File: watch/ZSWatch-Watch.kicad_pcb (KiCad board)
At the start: 4 copper layers, 37.4 x 37.5 mm, 62 parts, among them IC401 nPM1300-QEXX, IC501 APDS-9306-065, IC502 BMI270, IC503 LIS2MDLTR, IC504 BMP581, IC505 DRV2603RUNT, IC506 PCA9306JK, IC507 RV-8263-C8, IC601 FAN5622SX, IC602 USBLC6-2P6, IC603 MX25U51245GZ4I00, IC604 NTS0104GU12, M601 NORA-B106, X402 Battery, X509 Motor, X603 Device, X608 Display

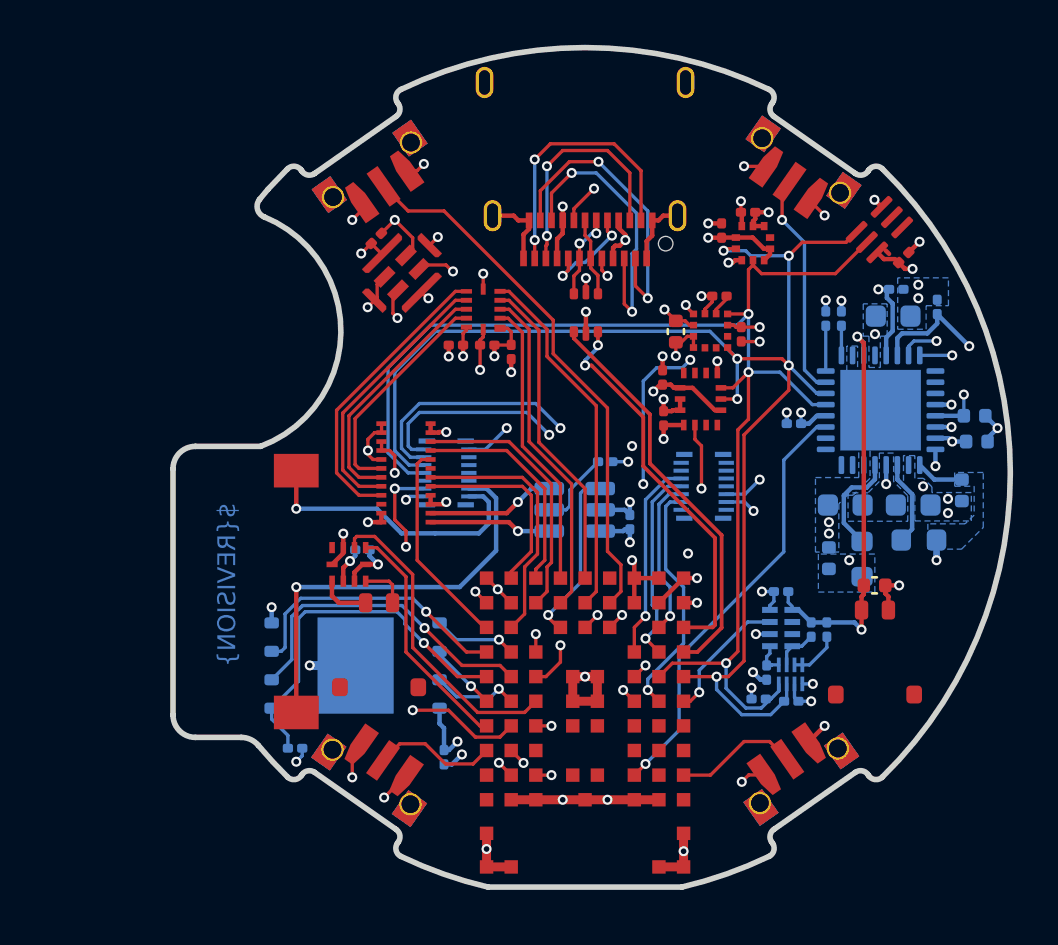
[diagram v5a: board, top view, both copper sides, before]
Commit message: New battery connector
- Add CI/CD workflow to check for changelog updates on pull requests

Signed-off-by: Daniel Kampert <DanielKampert|kampis-elektroecke.de>
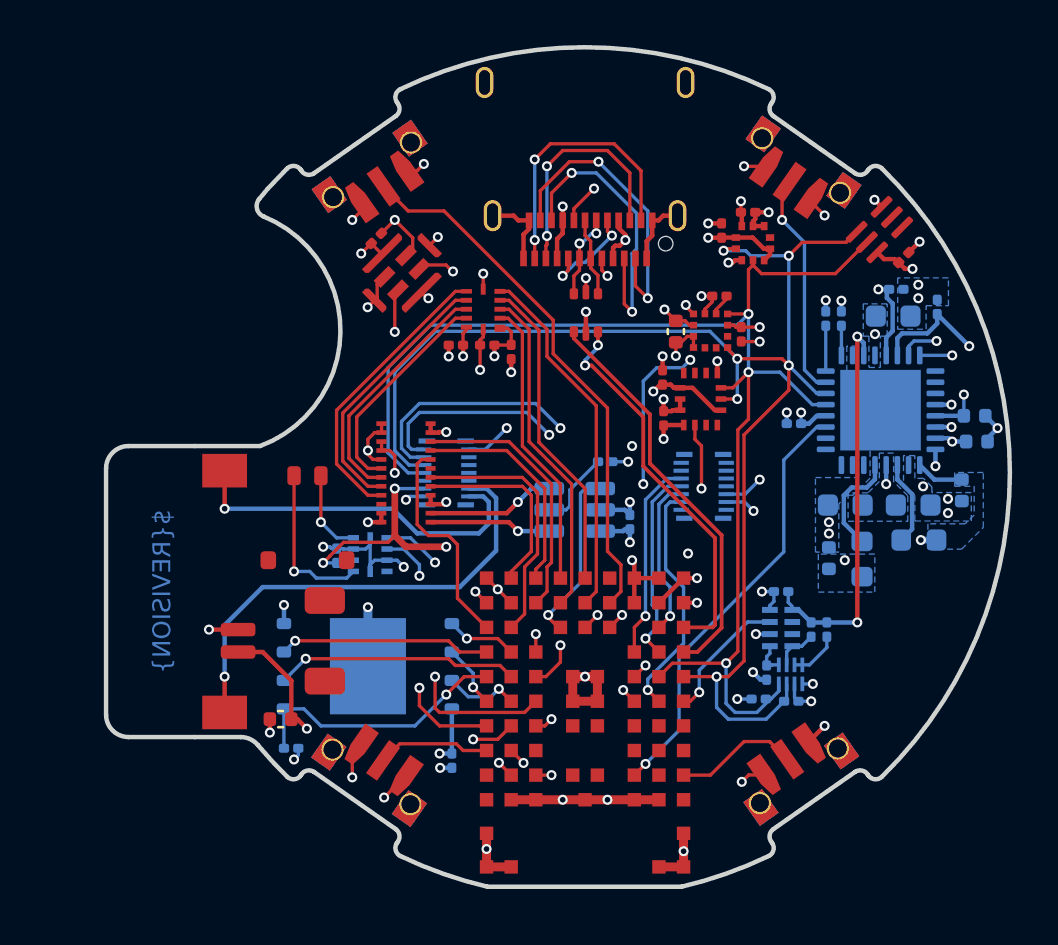
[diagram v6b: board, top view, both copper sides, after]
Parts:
- removed M801: ~, ZSWatch:Extension
- added X701: Conn_02x07_Odd_Even, Amphenol:101P014FB110, B.Cu at (212.3, 139.1)
- added X702: Conn_02x07_Odd_Even, Amphenol:101P014FB110, B.Cu at (200.8, 138.5)
- IC505: moved to B.Cu
- X402: footprint Molex:78171-0002 -> Connector_JST:JST_SH_SM02B-SRSS-TB_1x02-1MP_P1.00mm_Horizontal
- moved C403 27.2 mm to (193.4, 149.5), turned to 180 degrees
- moved X402 26.5 mm to (193.5, 146.0), turned to 90 degrees
- moved X509 6.52 mm to (194.6, 140.5)
- moved LS801 3.20 mm to (188.6, 143.8)
- moved C510 1.18 mm to (195.9, 142.2), turned to 90 degrees
- moved IC505 1.05 mm to (197.4, 142.2), turned to 180 degrees
- moved IC603 0.55 mm to (197.3, 147.1)
- moved C602 0.38 mm to (201.1, 151.4)
- moved R612 0.17 mm to (193.9, 150.8)
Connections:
- M601 pad F3: /Project Architecture/MCU/VIB-PWM -> /Project Architecture/MCU/VIB-EN
- M601 pad G1: /Project Architecture/MCU/VIB-EN -> /Project Architecture/MCU/VIB-PWM
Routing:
- net /Project Architecture/Peripherals/VBAT: track 24.8 -> 54.2 mm, vias 3 -> 4
- net /Project Architecture/MCU/MIC-DATA: track 30.2 -> 37.1 mm
- net Net-(IC505-OUT-): track 2.29 -> 7.17 mm, vias 0 -> 1
- net QSPI-CS: track 16.4 -> 12.0 mm
- net QSPI-IO1: track 14.5 -> 10.9 mm
- net /Project Architecture/MCU/MIC-CLK: track 30.2 -> 33.6 mm
- net /Project Architecture/MCU/VIB-EN: track 10.7 -> 13.9 mm, vias 0 -> 2
- net Net-(X702-Pin_2): track 12.9 -> 16.1 mm
- net QSPI-IO2: track 12.5 -> 9.46 mm
- net /Project Architecture/MCU/VIB-PWM: track 13.9 -> 11.4 mm, vias 0 -> 2
- net Net-(X702-Pin_4): track 18.9 -> 21.1 mm
- net GND: track 77.5 -> 79.2 mm, vias 60 -> 61
- net Net-(IC505-OUT+): track 2.07 -> 3.81 mm, vias 0 -> 1
- net /Project Architecture/Power Management/VSYS: track 57.6 -> 59.2 mm
- net /Project Architecture/Extension/SCL: track 63.7 -> 64.3 mm
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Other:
- board size 37.4 x 37.5 mm -> 40.4 x 37.5 mm
- board text added: "NOTE: The speaker will not be soldered. Instead the connections is pressure based which allows us to move the pins from the battery connector under the speaker"

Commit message: Replace wrong extension connectors
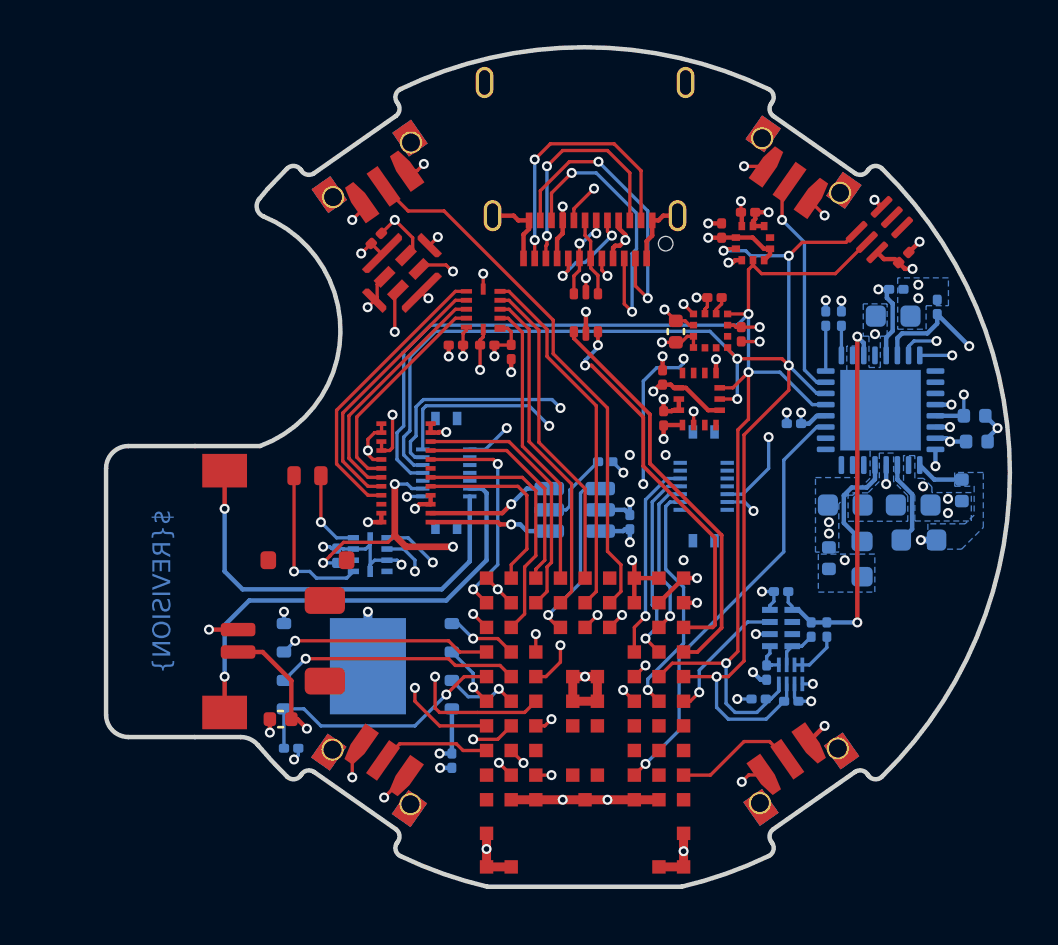
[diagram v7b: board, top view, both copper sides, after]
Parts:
- X701: value Conn_02x07_Odd_Even -> MB1; footprint Amphenol:101P014FB110 -> Amphenol:101R014FB110
- X702: value Conn_02x07_Odd_Even -> MB2; footprint Amphenol:101P014FB110 -> Amphenol:101R014FB110
- moved C505 0.23 mm to (212.8, 130.7)
- moved IC502 0.06 mm to (212.1, 135.2)
- turned X701 to 90 degrees
- turned X702 to -90 degrees
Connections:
- LS801 pad 1: Net-(X702-Pin_4) -> Net-(X702-Pin_3)
- LS801 pad 2: Net-(X702-Pin_2) -> Net-(X702-Pin_1)
- M601 pad B1: DISPLAY-EN -> DISPLAY-CLK
- M601 pad C1: DISPLAY-CLK -> DISPLAY-EN
- X701 pad 10: /Project Architecture/Extension/PA-DIN -> /Project Architecture/Extension/VPA
- X701 pad 11: GND -> /Project Architecture/Extension/PA-MCLK
- X701 pad 12: /Project Architecture/Extension/PA-MCLK -> GND
- X701 pad 5: unconnected-(X701-Pin_5-Pad5) -> /Project Architecture/Extension/PA-WCLK
- X701 pad 6: /Project Architecture/Extension/PA-WCLK -> unconnected-(X701-Pin_6-Pad6)
- X701 pad 7: unconnected-(X701-Pin_7-Pad7) -> /Project Architecture/Extension/PA-BCLK
- X701 pad 8: /Project Architecture/Extension/PA-BCLK -> unconnected-(X701-Pin_8-Pad8)
- X701 pad 9: /Project Architecture/Extension/VPA -> /Project Architecture/Extension/PA-DIN
- X702 pad 1: /Project Architecture/Extension/VHR -> Net-(X702-Pin_1)
- X702 pad 10: unconnected-(X702-Pin_10-Pad10) -> /Project Architecture/Extension/SCL
- X702 pad 11: /Project Architecture/Extension/Status -> unconnected-(X702-Pin_11-Pad11)
- X702 pad 12: unconnected-(X702-Pin_12-Pad12) -> /Project Architecture/Extension/Status
- X702 pad 13: /Project Architecture/Extension/~{RESET_{HR}} -> GND
- X702 pad 14: GND -> /Project Architecture/Extension/~{RESET_{HR}}
- X702 pad 2: Net-(X702-Pin_2) -> /Project Architecture/Extension/VHR
- X702 pad 3: /Project Architecture/Power Management/VSYS -> Net-(X702-Pin_3)
- X702 pad 4: Net-(X702-Pin_4) -> /Project Architecture/Power Management/VSYS
- X702 pad 7: /Project Architecture/Extension/SDA -> unconnected-(X702-Pin_7-Pad7)
- X702 pad 8: unconnected-(X702-Pin_8-Pad8) -> /Project Architecture/Extension/SDA
- X702 pad 9: /Project Architecture/Extension/SCL -> unconnected-(X702-Pin_9-Pad9)
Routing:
- net Net-(X702-Pin_4): track 21.1 -> 0.00 mm, vias 1 -> 0
- net Net-(X702-Pin_3): track 0.00 -> 20.7 mm, vias 0 -> 1
- net Net-(X702-Pin_1): track 0.00 -> 19.2 mm, vias 0 -> 1
- net Net-(X702-Pin_2): track 16.1 -> 0.00 mm, vias 1 -> 0
- net /Project Architecture/Extension/VHR: track 52.0 -> 48.6 mm, vias 4 -> 5
- net +3V0: track 46.2 -> 47.7 mm
- net /Project Architecture/Power Management/VSYS: track 59.2 -> 60.5 mm
- net /Project Architecture/Extension/VPA: track 14.6 -> 13.4 mm
- net DISPLAY-EN: track 12.8 -> 14.0 mm
- net /Project Architecture/MCU/BMI270-INT: track 12.6 -> 13.6 mm
- net DISPLAY-CLK: track 9.79 -> 9.99 mm, vias 0 -> 2

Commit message: OPtimize connector positions
- New position for the battery connector, moved to the right side of the watch
- Rotate haptics connector by 180°
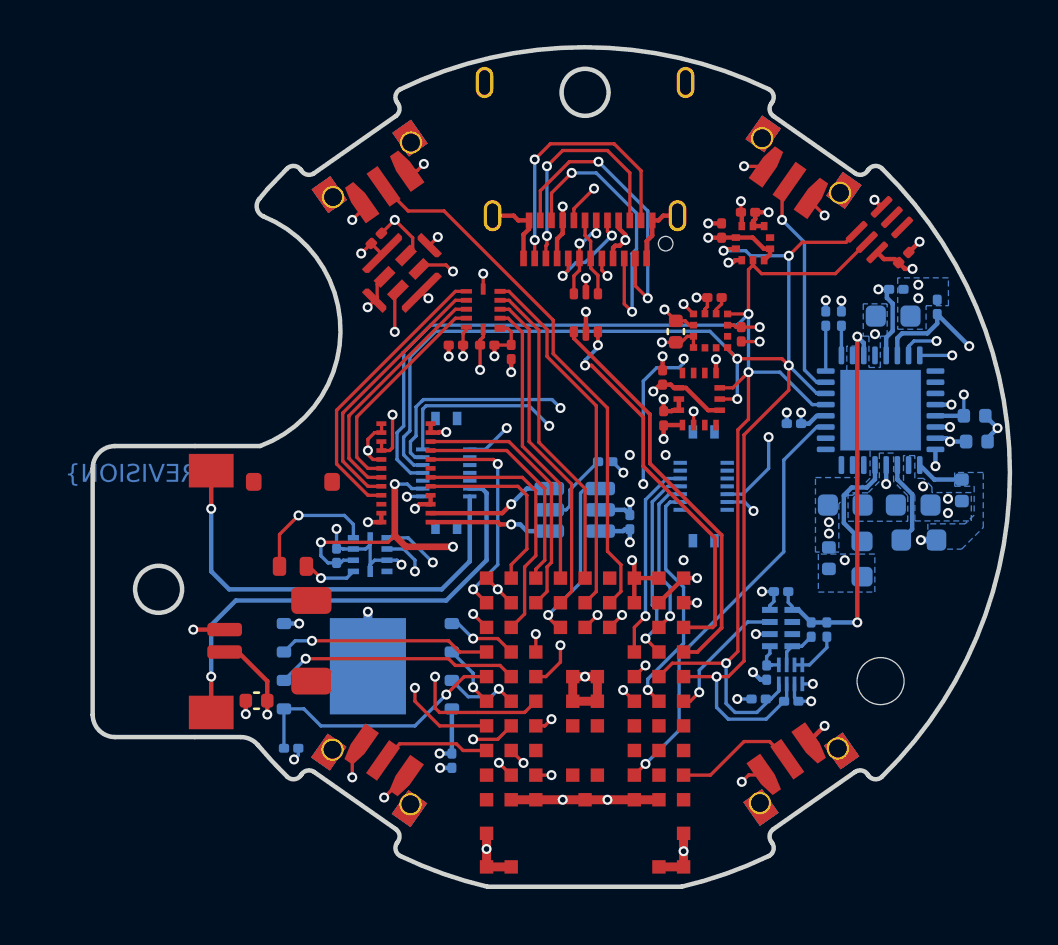
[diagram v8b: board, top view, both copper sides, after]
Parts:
- added REF**: MountingHole_2.1mm, MountingHole:MountingHole_2.1mm, F.Cu at (220.2, 147.8)
- moved C403 1.36 mm to (192.3, 148.7)
- moved X509 0.72 mm to (193.9, 140.8), turned to 180 degrees
- moved LS801 0.60 mm to (188.0, 143.8)
- moved X402 0.60 mm to (192.9, 146.0)
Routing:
- net Net-(IC505-OUT-): track 7.17 -> 2.44 mm
- net Net-(IC505-OUT+): track 3.81 -> 5.84 mm
- net /Project Architecture/Power Management/VSYS: track 60.5 -> 59.2 mm
- net GND: track 79.1 -> 80.2 mm
- net Net-(X702-Pin_3): track 20.7 -> 21.3 mm
- net Net-(X702-Pin_1): track 19.2 -> 19.8 mm
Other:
- board size 40.4 x 37.5 mm -> 41 x 37.5 mm
